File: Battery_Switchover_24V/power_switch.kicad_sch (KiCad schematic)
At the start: 1 part, among them U3 LPC11U14FBD48-201

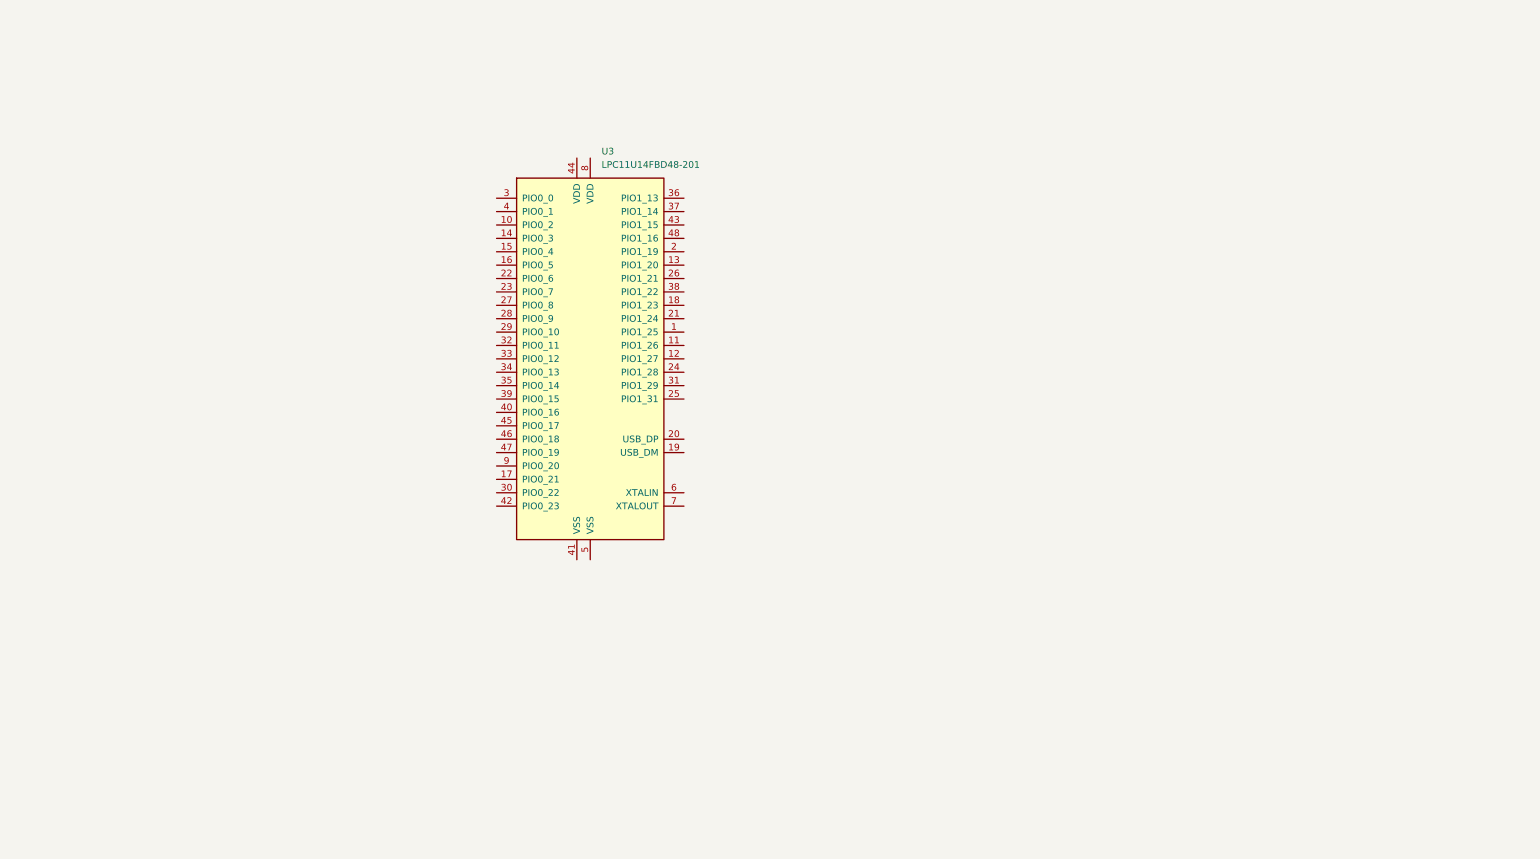
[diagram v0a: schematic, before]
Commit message: Voltaj denetim çipi eklendi
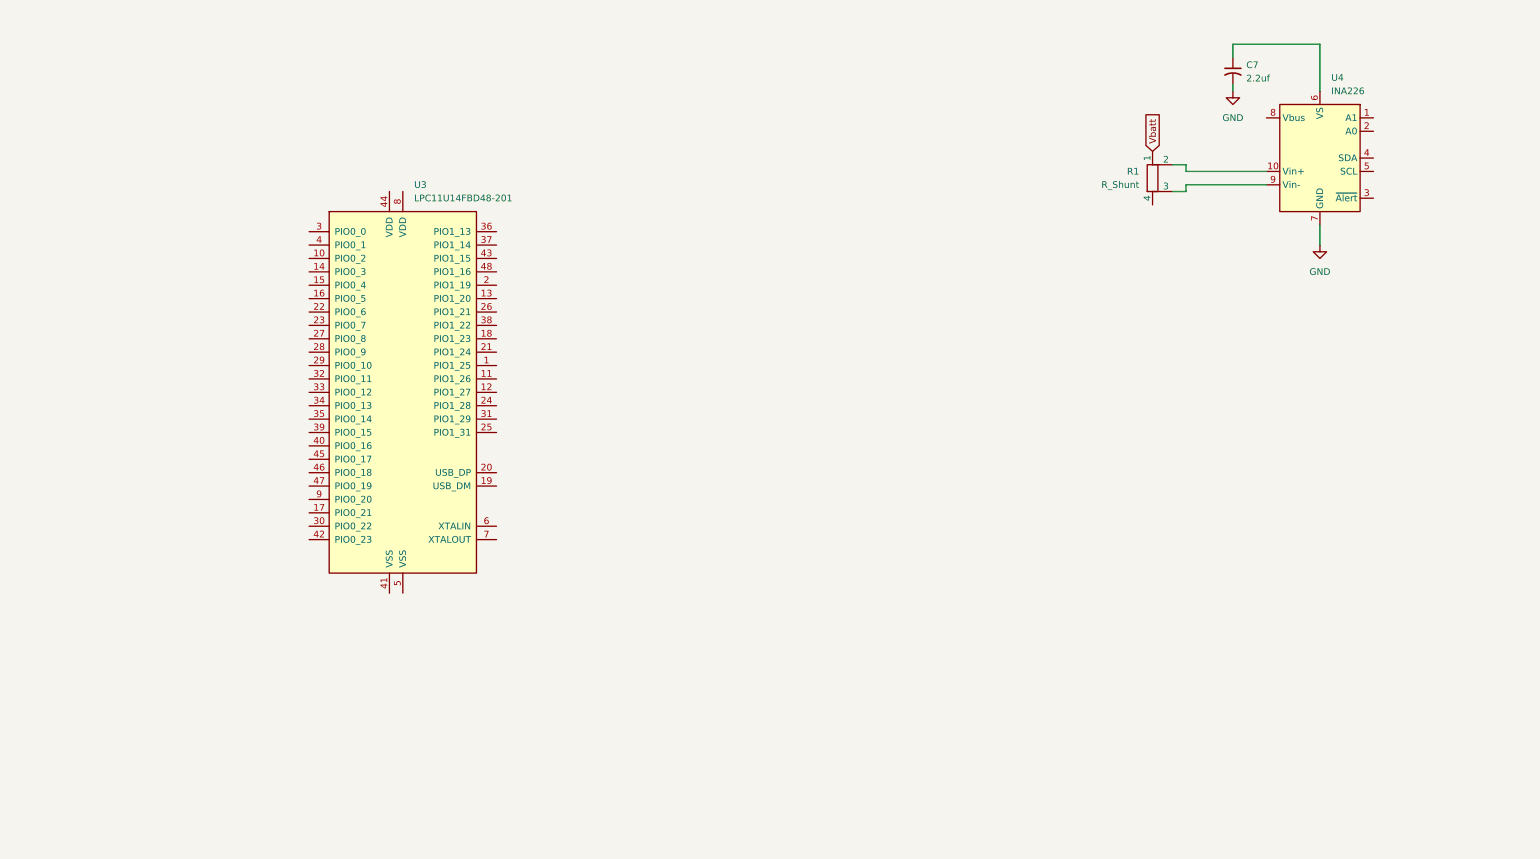
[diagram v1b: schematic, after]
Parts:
- added C7: 2.2uf, symbol Device:C_Small_US
- added R1: R_Shunt, symbol Device:R_Shunt
- added U4: INA226, Package_SO:VSSOP-10_3x3mm_P0.5mm, symbol Sensor_Energy:INA226
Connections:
- new net: C7.1, U4.6 (VS)
- new net: R1.2, U4.10 (Vin+)
- new net: R1.3, U4.9 (Vin-)
- new net GND: C7.2, U4.7 (GND)
- new net Vbatt: R1.1
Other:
- moved on the sheet: U3

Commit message: Changer Voltage Detection
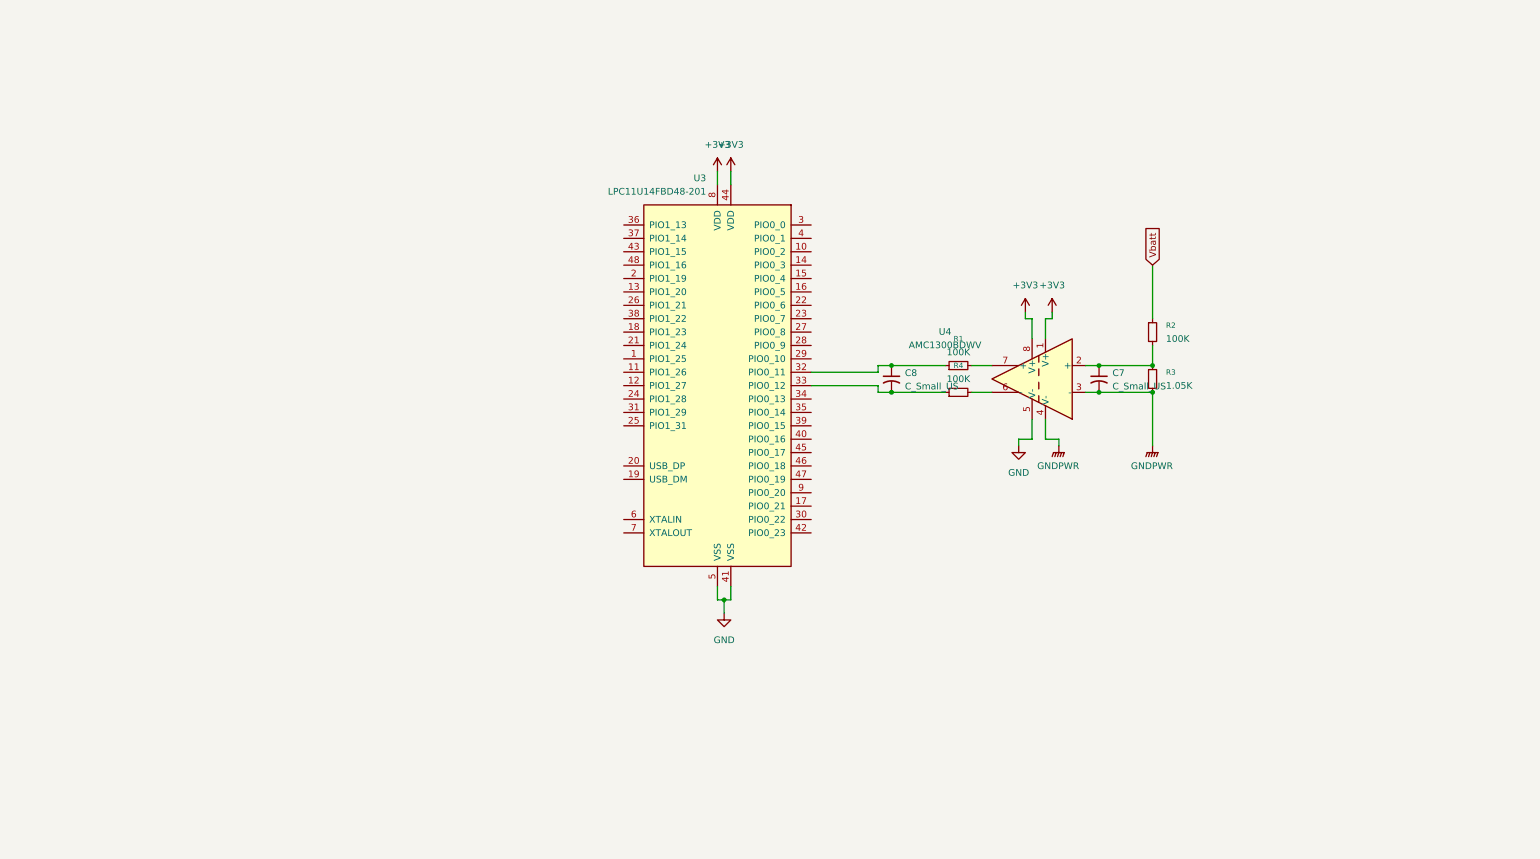
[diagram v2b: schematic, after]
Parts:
- removed R1: R_Shunt, symbol Device:R_Shunt
- removed U4: INA226, Package_SO:VSSOP-10_3x3mm_P0.5mm, symbol Sensor_Energy:INA226
- added C8: C_Small_US, symbol Device:C_Small_US
- added R1, R2, R4: 100K, symbol Device:R_Small
- added R3: 1.05K, symbol Device:R_Small
- added U4: AMC1300BDWV, Package_SO:SOIC-8_7.5x5.85mm_P1.27mm, symbol Amplifier_Difference:AMC1300BDWV
- C7: value 2.2uf -> C_Small_US
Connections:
- net GND: now also U3.41 (VSS), U3.5 (VSS), U4.5 (V-); no longer C7.2
- net Vbatt: now also R2.1
- net at C7.1: now also R2.2, R3.1, U4.2 (+)
- net at U3.32 (PIO0_11): now also C8.1, R1.1
- net at U3.33 (PIO0_12): now also C8.2, R4.1
- net +3V3: now reaches U3.44 (VDD)
- net +3V3: now also U3.8 (VDD), U4.1 (V+), U4.8 (V+)
- new net: R1.2, U4.7 (+)
- new net: R4.2, U4.6 (-)
- new net GNDPWR: C7.2, R3.2, U4.3 (-), U4.4 (V-)
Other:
- moved on the sheet: U3

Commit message: Added USB connection
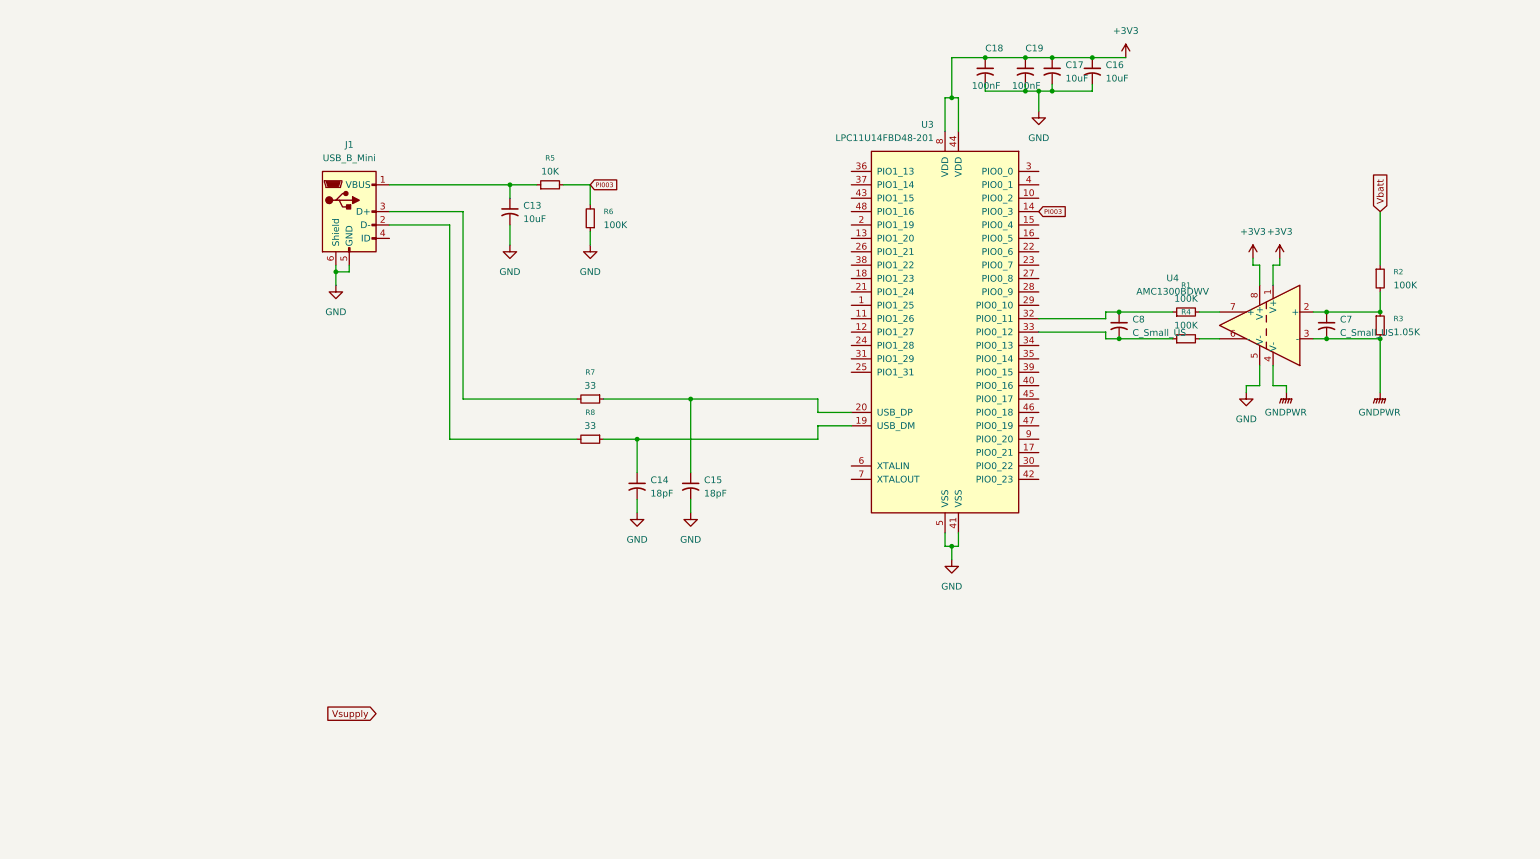
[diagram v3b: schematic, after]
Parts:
- added C13, C16, C17: 10uF, symbol Device:C_Small_US
- added C14, C15: 18pF, symbol Device:C_Small_US
- added C18, C19: 100nF, symbol Device:C_Small_US
- added J1: USB_B_Mini, symbol Connector:USB_B_Mini
- added R5: 10K, symbol Device:R_Small
- added R6: 100K, symbol Device:R_Small
- added R7, R8: 33, symbol Device:R_Small
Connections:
- net +3V3: now also C16.1, C17.1, C18.1, C19.1
- net GND: now also C13.2, C14.2, C15.2, C16.2, C17.2, C18.2, C19.2, J1.5 (GND), J1.6 (Shield), R6.1
- net PI003: now reaches U3.14 (PIO0_3)
- net PI003: now also R5.2, R6.2
- net at U3.19 (USB_DM): now also C14.1, R8.1
- net at U3.20 (USB_DP): now also C15.1, R7.1
- new net: J1.2 (D-), R8.2
- new net: C13.1, J1.1 (VBUS), R5.1
- new net: J1.3 (D+), R7.2
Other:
- moved on the sheet: C7, C8, R1, R2, R3, R4, U3, U4

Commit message: Akım devresi eklendi Diğer devrelerde değişikler yapıldı
24 volttan tps54560 ile 5V oradan linear regulator ile 3.3V dönüştürüldü.

LPC11U14 e cristal eklendi
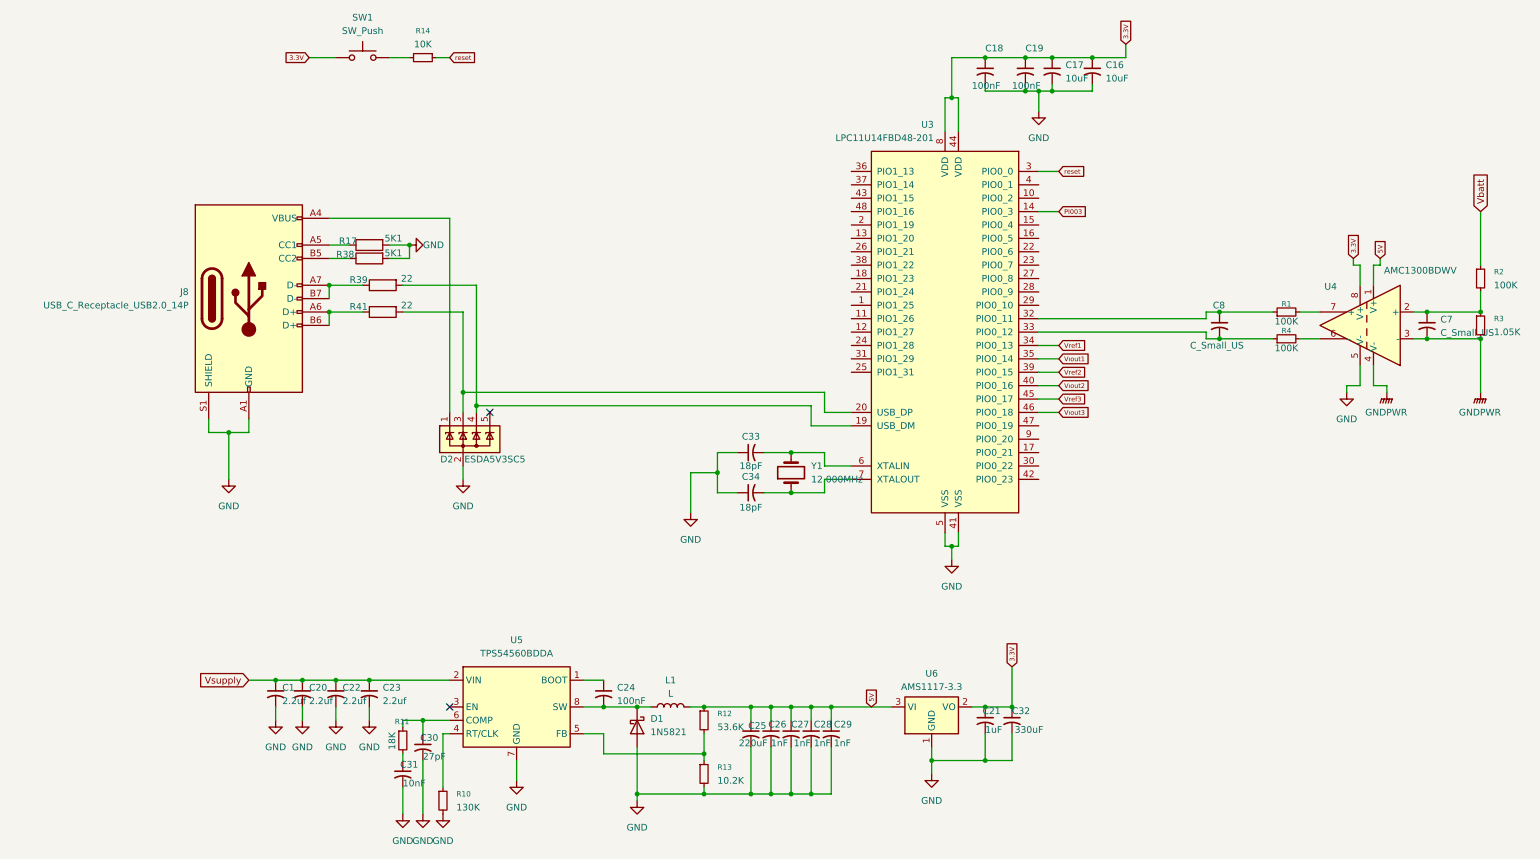
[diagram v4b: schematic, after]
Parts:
- removed C13: 10uF, symbol Device:C_Small_US
- removed C14, C15: 18pF, symbol Device:C_Small_US
- removed J1: USB_B_Mini, symbol Connector:USB_B_Mini
- removed R5: 10K, symbol Device:R_Small
- removed R6: 100K, symbol Device:R_Small
- removed R7, R8: 33, symbol Device:R_Small
- added C1, C20, C22, C23: 2.2uf, symbol Device:C_Small_US
- added C21: 1uF, symbol Device:C_Small_US
- added C24: 100nF, symbol Device:C_Small_US
- added C25: 220uF, symbol Device:C_Small_US
- added C26, C27, C28, C29: 1nF, symbol Device:C_Small_US
- added C30: 27pF, symbol Device:C_Small_US
- added C31: 10nF, symbol Device:C_Small_US
- added C32: 330uF, symbol Device:C_Small_US
- added C33, C34: 18pF, symbol Device:C_Small_US
- added D1: 1N5821, Diode_THT:D_DO-201AD_P15.24mm_Horizontal, symbol Diode:1N5821
- added D2: ESDA5V3SC5, Package_TO_SOT_SMD:SOT-23-5, symbol Power_Protection:ESDA5V3SC5
- added J8: USB_C_Receptacle_USB2.0_14P, Connector_USB:USB_C_Receptacle_G-Switch_GT-USB-7010ASV, symbol Connector:USB_C_Receptacle_USB2.0_14P
- added L1: L, symbol Device:L
- added R10: 130K, symbol Device:R_Small
- added R11: 18K, symbol Device:R_Small
- added R12: 53.6K, symbol Device:R_Small
- added R13: 10.2K, symbol Device:R_Small
- added R14: 10K, symbol Device:R_Small
- added R17, R38: 5K1, Resistor_SMD:R_0603_1608Metric, symbol Device:R
- added R39, R41: 22, Resistor_SMD:R_0603_1608Metric, symbol Device:R
- added SW1: SW_Push, symbol changes:SW_Push
- added U5: TPS54560BDDA, Package_SO:Texas_R-PDSO-G8_EP2.95x4.9mm_Mask2.4x3.1mm_ThermalVias, symbol Regulator_Switching:TPS54560BDDA
- added U6: AMS1117-3.3, Package_TO_SOT_SMD:SOT-223-3_TabPin2, symbol Regulator_Linear:AMS1117-3.3
- added Y1: 12.000MHz, symbol Device:Crystal
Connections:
- net GND: now also C1.2, C20.2, C21.2, C22.2, C23.2, C25.2, C26.2, C27.2, C28.2, C29.2, C30.2, C31.2, C32.2, C33.1, C34.1, D1.2 (A), D2.2 (A), J8.A1 (GND), J8.A12 (GND), J8.B1 (GND), J8.B12 (GND), J8.S1 (SHIELD), R10.2, R13.2, R17.2, R38.2, U5.7 (GND), U5.9 (GND), U6.1 (GND)
- net Vsupply: now also C1.1, C20.1, C22.1, C23.1, U5.2 (VIN)
- net at U3.19 (USB_DM): now also D2.4 (K), R39.2
- net at U3.20 (USB_DP): now also D2.3 (K), R41.2
- net reset: now reaches U3.3 (PIO0_0)
- net reset: now also R14.1
- net Vref1: now reaches U3.34 (PIO0_13)
- net Vıout1: now reaches U3.35 (PIO0_14)
- net Vref2: now reaches U3.39 (PIO0_15)
- net Vıout2: now reaches U3.40 (PIO0_16)
- net Vref3: now reaches U3.45 (PIO0_17)
- net Vıout3: now reaches U3.46 (PIO0_18)
- net at U3.6 (XTALIN): now also C33.2, Y1.2
- net at U3.7 (XTALOUT): now also C34.2, Y1.1
- net +3V3 renamed 3.3V
- net 3.3V: now also C21.1, C32.1, SW1.1, U6.2 (VO); no longer U4.1 (V+)
- new net: C24.2, D1.1 (K), L1.1, U5.8 (SW)
- new net: J8.A6 (D+), J8.B6 (D+), R41.1
- new net: J8.B5 (CC2), R38.1
- new net: C24.1, U5.1 (BOOT)
- new net: R10.1, U5.4 (RT/CLK)
- new net: R12.2, R13.1, U5.5 (FB)
- new net: C30.1, R11.1, U5.6 (COMP)
- new net: C31.1, R11.2
- new net: J8.A5 (CC1), R17.1
- new net: R14.2, SW1.2
- new net: D2.1 (K), J8.A4 (VBUS), J8.A9 (VBUS), J8.B4 (VBUS), J8.B9 (VBUS)
- new net: J8.A7 (D-), J8.B7 (D-), R39.1
- new net 5V: C25.1, C26.1, C27.1, C28.1, C29.1, L1.2, R12.1, U4.1 (V+), U6.3 (VI)
- no-connect marks 0 -> 2
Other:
- moved on the sheet: C7, C8, R1, R2, R3, R4, U4
